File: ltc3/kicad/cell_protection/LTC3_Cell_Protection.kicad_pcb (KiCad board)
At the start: 4 copper layers, 70 parts, among them P1 S2BPHKS, P2 PIN_HEAD_1x2, P3 CONN_BATT_MAIN, P4 CONN_BATT_SENSE, Q1 SUM110P08-11, Q2 SUM110P08-11, Q3 NDS9407, Q4 SUM110P08-11, Q5 SUM110P08-11, Q6 MMBT3904, U1 BQ77PL900, U2 LTC2990

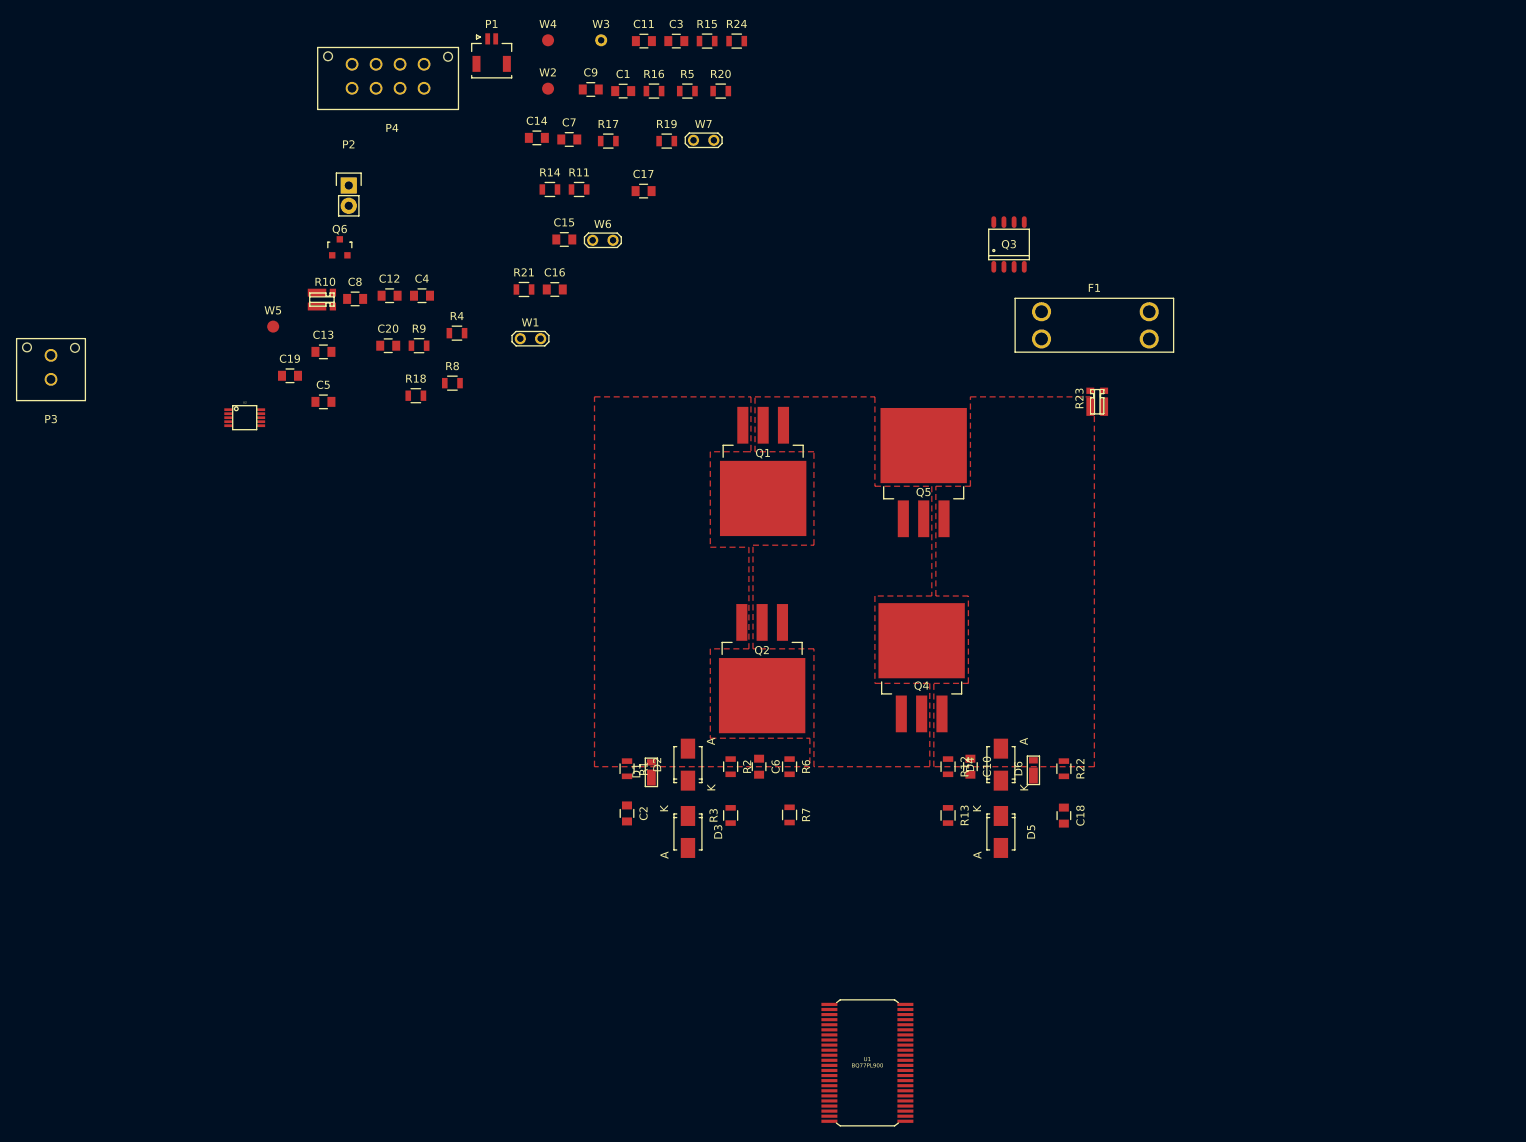
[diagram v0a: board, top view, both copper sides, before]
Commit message: LTC3: Continued layout work
Continued work on cell protection layout.
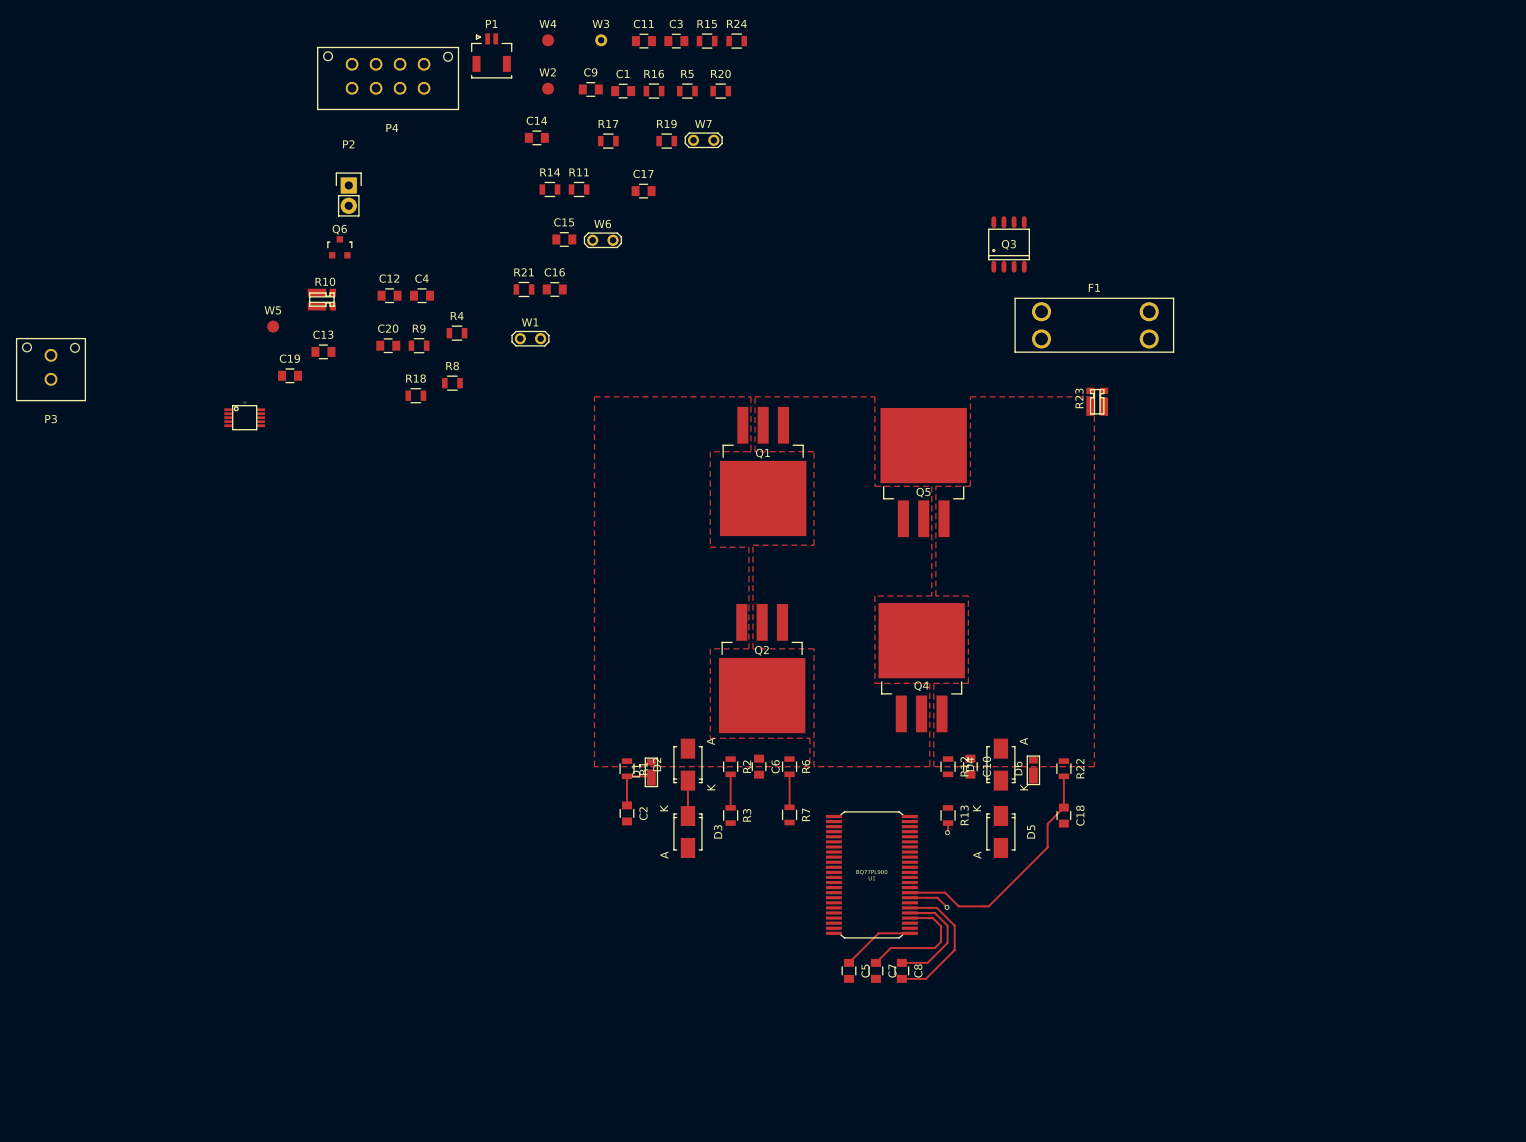
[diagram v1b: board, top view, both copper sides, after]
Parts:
- moved C7 110.8 mm to (124.1, 130.7), turned to 270 degrees
- moved C8 108.3 mm to (127.3, 130.7), turned to 270 degrees
- moved C5 96.8 mm to (120.7, 130.7), turned to 270 degrees
- moved U1 23.5 mm to (123.6, 118.7), turned to 180 degrees
- turned R3 to 270 degrees
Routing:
- net Net-(C18-Pad1): track 0.00 -> 30.7 mm
- net Net-(C8-Pad2): track 0.00 -> 17.7 mm
- net Net-(R13-Pad2): track 0.00 -> 15.7 mm, vias 0 -> 2
- net Net-(C7-Pad1): track 0.00 -> 15.5 mm
- net Net-(C8-Pad1): track 0.00 -> 14.3 mm
- net Net-(C5-Pad1): track 0.00 -> 9.14 mm
- net Net-(C2-Pad1): track 0.00 -> 6.75 mm
- net Net-(D2-Pad1): track 0.00 -> 4.42 mm
- net Net-(Q3-Pad4): track 0.00 -> 4.20 mm
- net Net-(C6-Pad2): track 0.00 -> 4.13 mm
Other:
- net class Default: clearance 0.2 -> 0.1238
- rule trace_clearance: 0.2 -> 0.1238

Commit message: LTC3 Layout:
Continued layout of Cell Protection circuitry.
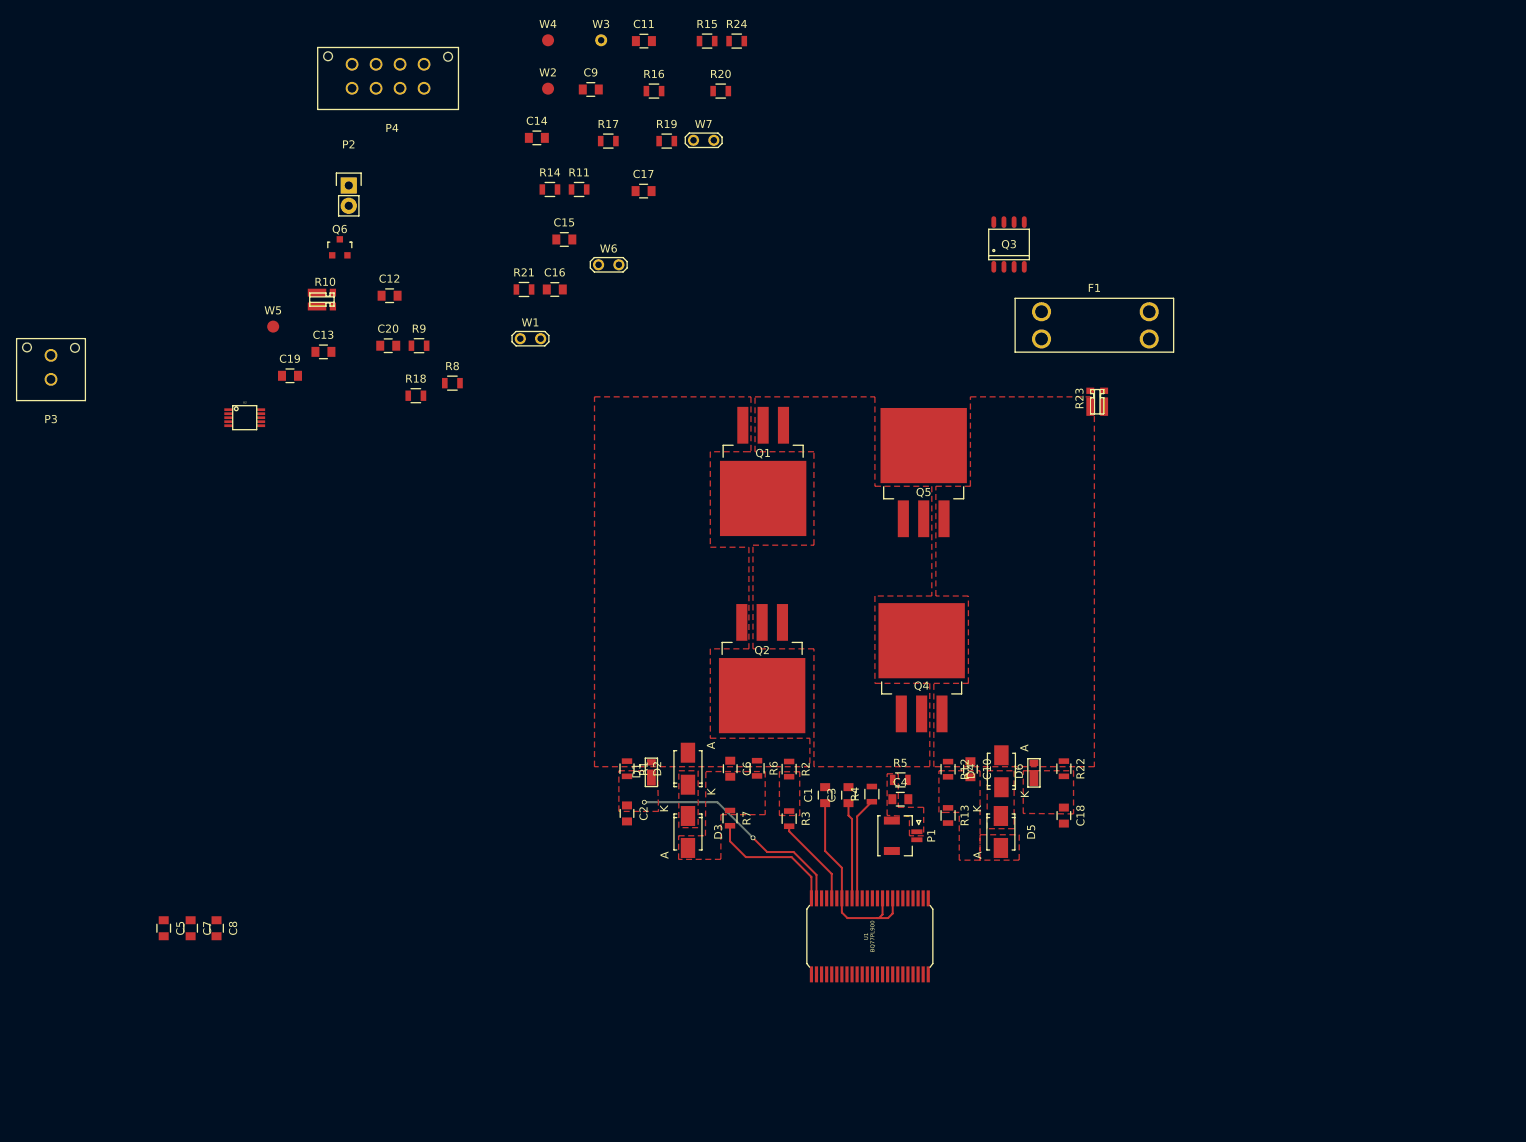
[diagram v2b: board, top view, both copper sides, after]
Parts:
- moved P1 110.8 mm to (127.6, 113.8), turned to 270 degrees
- moved C3 96.7 mm to (120.7, 108.7), turned to 90 degrees
- moved C1 91.6 mm to (117.7, 108.7), turned to 90 degrees
- moved R5 90.1 mm to (127.1, 106.8)
- moved C4 86.8 mm to (127.1, 109.2)
- moved C5 85.8 mm to (35.1, 125.3)
- moved C7 85.8 mm to (38.4, 125.3)
- moved C8 85.8 mm to (41.7, 125.3)
- moved R4 77.5 mm to (123.6, 108.6), turned to 90 degrees
- moved U1 7.69 mm to (123.3, 126.4), turned to 90 degrees
- moved R7 7.45 mm to (105.8, 111.6)
- moved R3 7.33 mm to (113.2, 111.7)
- moved R2 7.32 mm to (113.2, 105.5)
- moved R6 4.07 mm to (109.2, 105.4)
- moved C6 3.62 mm to (105.9, 105.4)
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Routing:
- net Net-(C18-Pad1): track 30.7 -> 0.00 mm
- net Net-(C1-Pad1): track 0.00 -> 26.2 mm
- net Net-(C2-Pad1): track 6.75 -> 28.2 mm, vias 0 -> 2
- net Net-(C8-Pad2): track 17.7 -> 0.00 mm
- net Net-(R7-Pad2): track 0.00 -> 16.6 mm
- net Net-(R13-Pad2): track 15.7 -> 0.00 mm, vias 2 -> 0
- net Net-(C7-Pad1): track 15.5 -> 0.00 mm
- net Net-(C8-Pad1): track 14.3 -> 0.00 mm
- net Net-(R4-Pad1): track 0.00 -> 12.8 mm
- net Net-(C3-Pad1): track 0.00 -> 12.1 mm
- net Net-(R3-Pad2): track 0.00 -> 11.2 mm
- net Net-(C5-Pad1): track 9.14 -> 0.00 mm
- net Net-(D2-Pad1): track 4.42 -> 0.00 mm
- net Net-(Q3-Pad4): track 4.20 -> 0.00 mm
- net Net-(C6-Pad2): track 4.13 -> 0.00 mm
- added copper zone on F.Cu, net Net-(C10-Pad2)
- added copper zone on F.Cu, net Net-(C18-Pad1)
- added copper zone on F.Cu, net Net-(C2-Pad1)
- added copper zone on F.Cu, net Net-(C4-Pad1)
- added copper zone on F.Cu, net Net-(C6-Pad2)
- added copper zone on F.Cu, net Net-(D2-Pad1)
- added copper zone on F.Cu, net Net-(D4-Pad1)
- added copper zone on F.Cu, net Net-(Q3-Pad4)

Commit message: LTC3: Layout Con't
I spent like 5 minutes on this commit and got kind of frustrated.  Not
much in here.
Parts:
- moved Q1 7.11 mm to (110.0, 69.6)
- moved Q5 5.85 mm to (130.0, 80.0)
- moved R23 5.64 mm to (152.4, 65.8)
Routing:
- net Net-(C4-Pad1): track 0.00 -> 14.2 mm
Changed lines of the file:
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@@
     (thickness 1.6)
     (drawings 0)
-    (tracks 33)
+    (tracks 36)
     (zones 0)
     (modules 70)
@@
   )
   (module TO_SOT_Packages_SMD:TO-263-3Lead (layer F.Cu)
-    (at 109.982 62.478 270)
+    (at 109.982 69.59 270)
     (descr "D2PAK / TO-263 3-lead smd package")
     (tags "D2PAK D2PAK-3 TO-263AB TO-263")
@@
   )
   (module TO_SOT_Packages_SMD:TO-263-3Lead (layer F.Cu)
-    (at 130.048 74.168 90)
+    (at 130.048 80.016 90)
     (descr "D2PAK / TO-263 3-lead smd package")
     (tags "D2PAK D2PAK-3 TO-263AB TO-263")
@@
   )
   (module LTC3:CST0612 (layer F.Cu)
-    (at 152.6032 60.1726 90)
+    (at 152.4 65.8114 90)
     (descr "Bourns CST0612 Current Sense Resistor")
     (tags "resistor current sense shunt 0612")
@@
   (segment (start 120.65 111.252) (end 120.65 109.712) (width 0.25) (layer F.Cu) (net 4))
   (segment (start 121.0945 111.6965) (end 120.65 111.252) (width 0.25) (layer F.Cu) (net 4))
+  (segment (start 122.3645 121.615) (end 122.3645 114.8715) (width 0.25) (layer F.Cu) (net 5))
+  (segment (start 123.944 113.292) (end 129.1975 113.292) (width 0.25) (layer F.Cu) (net 5))
+  (segment (start 122.3645 114.8715) (end 123.944 113.292) (width 0.25) (layer F.Cu) (net 5))
   (segment (start 113.2332 112.6) (end 113.2332 113.2332) (width 0.25) (layer F.Cu) (net 37))
   (segment (start 118.5545 118.5545) (end 118.5545 121.615) (width 0.25) (layer F.Cu) (net 37))
@@
         (xy 108.204 65.786) (xy 103.378 65.786) (xy 103.378 77.724) (xy 108.204 77.724) (xy 108.204 90.424)
         (xy 103.378 90.424) (xy 103.378 101.6) (xy 115.824 101.6) (xy 115.824 105.156) (xy 88.9 105.156)
-        (xy 88.9 58.928) (xy 108.458 58.928) (xy 108.458 65.786)
+        (xy 88.9 64.516) (xy 108.458 64.516) (xy 108.458 65.786)
       )
     )
@@
       (pts
         (xy 108.712 90.424) (xy 108.712 77.47) (xy 116.332 77.47) (xy 116.332 65.786) (xy 108.966 65.786)
-        (xy 108.966 58.928) (xy 123.952 58.928) (xy 123.952 70.104) (xy 131.064 70.104) (xy 131.064 83.82)
+        (xy 108.966 64.516) (xy 124.333 64.516) (xy 124.333 70.104) (xy 131.064 70.104) (xy 131.064 83.82)
         (xy 123.952 83.82) (xy 123.952 94.742) (xy 130.81 94.742) (xy 130.81 105.156) (xy 116.332 105.156)
         (xy 116.332 90.424)
@@
       (pts
         (xy 131.318 105.156) (xy 131.318 94.742) (xy 135.636 94.742) (xy 135.636 83.82) (xy 131.572 83.82)
-        (xy 131.572 70.104) (xy 135.89 70.104) (xy 135.89 58.928) (xy 151.384 58.928) (xy 151.384 105.156)
+        (xy 131.572 70.104) (xy 135.89 70.104) (xy 135.89 64.516) (xy 151.384 64.516) (xy 151.384 105.156)
       )
     )
@@
     (polygon
       (pts
-        (xy 126.873 110.236) (xy 130.048 110.236) (xy 130.048 113.792) (xy 128.27 113.792) (xy 128.27 111.379)
-        (xy 125.476 111.252) (xy 125.476 106.045) (xy 126.873 106.045) (xy 126.873 110.236)
+        (xy 126.873 110.236) (xy 130.048 110.236) (xy 130.048 113.792) (xy 128.27 113.792) (xy 128.27 111.252)
+        (xy 125.476 111.252) (xy 125.476 108.458) (xy 122.809 108.458) (xy 122.809 106.045) (xy 126.873 106.045)
+        (xy 126.873 110.236)
       )
     )

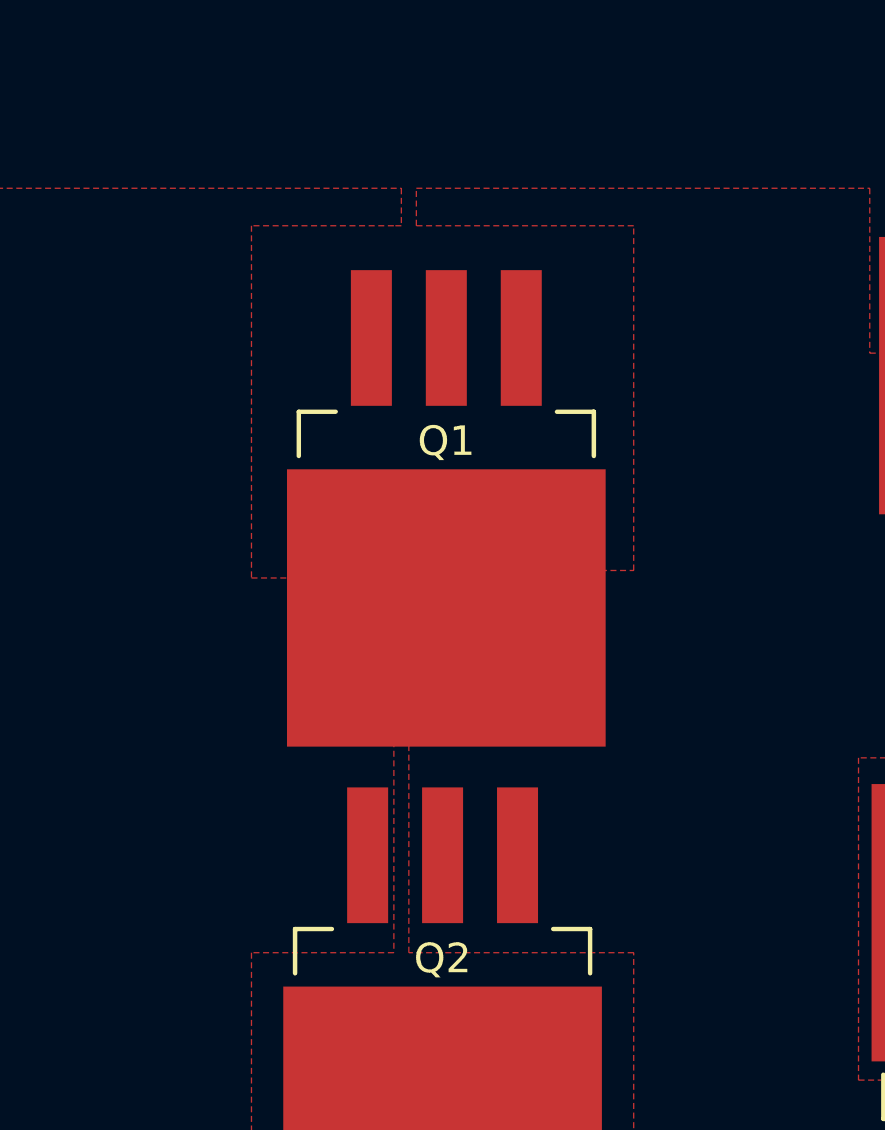
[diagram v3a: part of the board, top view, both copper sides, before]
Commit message: LTC3: Reworking Charge Controller Layout
- Assigned correct footprints to LEDs, Fuse, output connector
- Reworked high current polygons
- Added mounting holes

Still more work to be done.
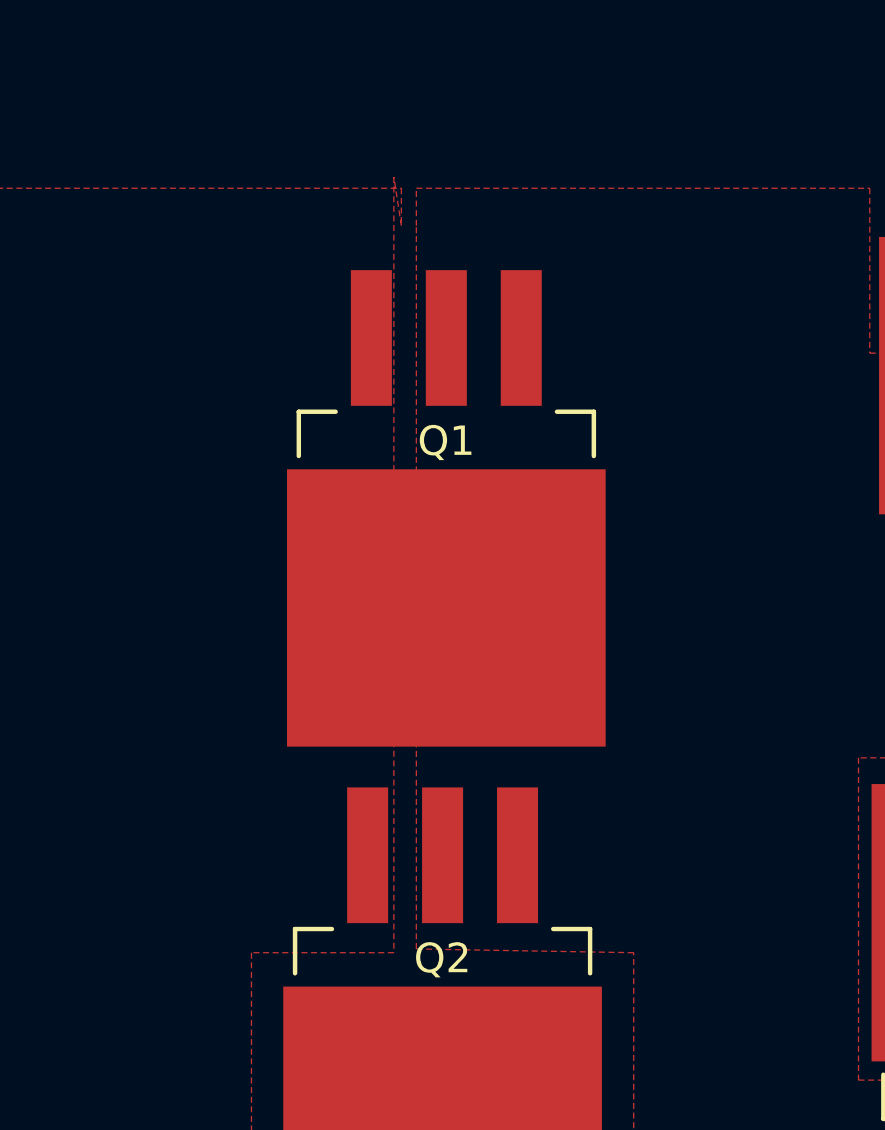
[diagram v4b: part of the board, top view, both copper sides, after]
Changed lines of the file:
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@@
     (polygon
       (pts
-        (xy 108.204 65.786) (xy 103.378 65.786) (xy 103.378 77.724) (xy 108.204 77.724) (xy 108.204 90.424)
+        (xy 108.458 65.786) (xy 108.204 64.135) (xy 108.204 76.073) (xy 108.204 77.724) (xy 108.204 90.424)
         (xy 103.378 90.424) (xy 103.378 101.6) (xy 115.824 101.6) (xy 115.824 105.156) (xy 88.9 105.156)
         (xy 88.9 64.516) (xy 108.458 64.516) (xy 108.458 65.786)
@@
     (polygon
       (pts
-        (xy 108.712 90.424) (xy 108.712 77.47) (xy 116.332 77.47) (xy 116.332 65.786) (xy 108.966 65.786)
+        (xy 108.966 90.297) (xy 108.966 77.343) (xy 108.966 77.724) (xy 108.966 66.04) (xy 108.966 65.786)
         (xy 108.966 64.516) (xy 124.333 64.516) (xy 124.333 70.104) (xy 131.064 70.104) (xy 131.064 83.82)
         (xy 123.952 83.82) (xy 123.952 94.742) (xy 130.81 94.742) (xy 130.81 105.156) (xy 116.332 105.156)
